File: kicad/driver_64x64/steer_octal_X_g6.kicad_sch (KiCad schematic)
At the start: 66 parts

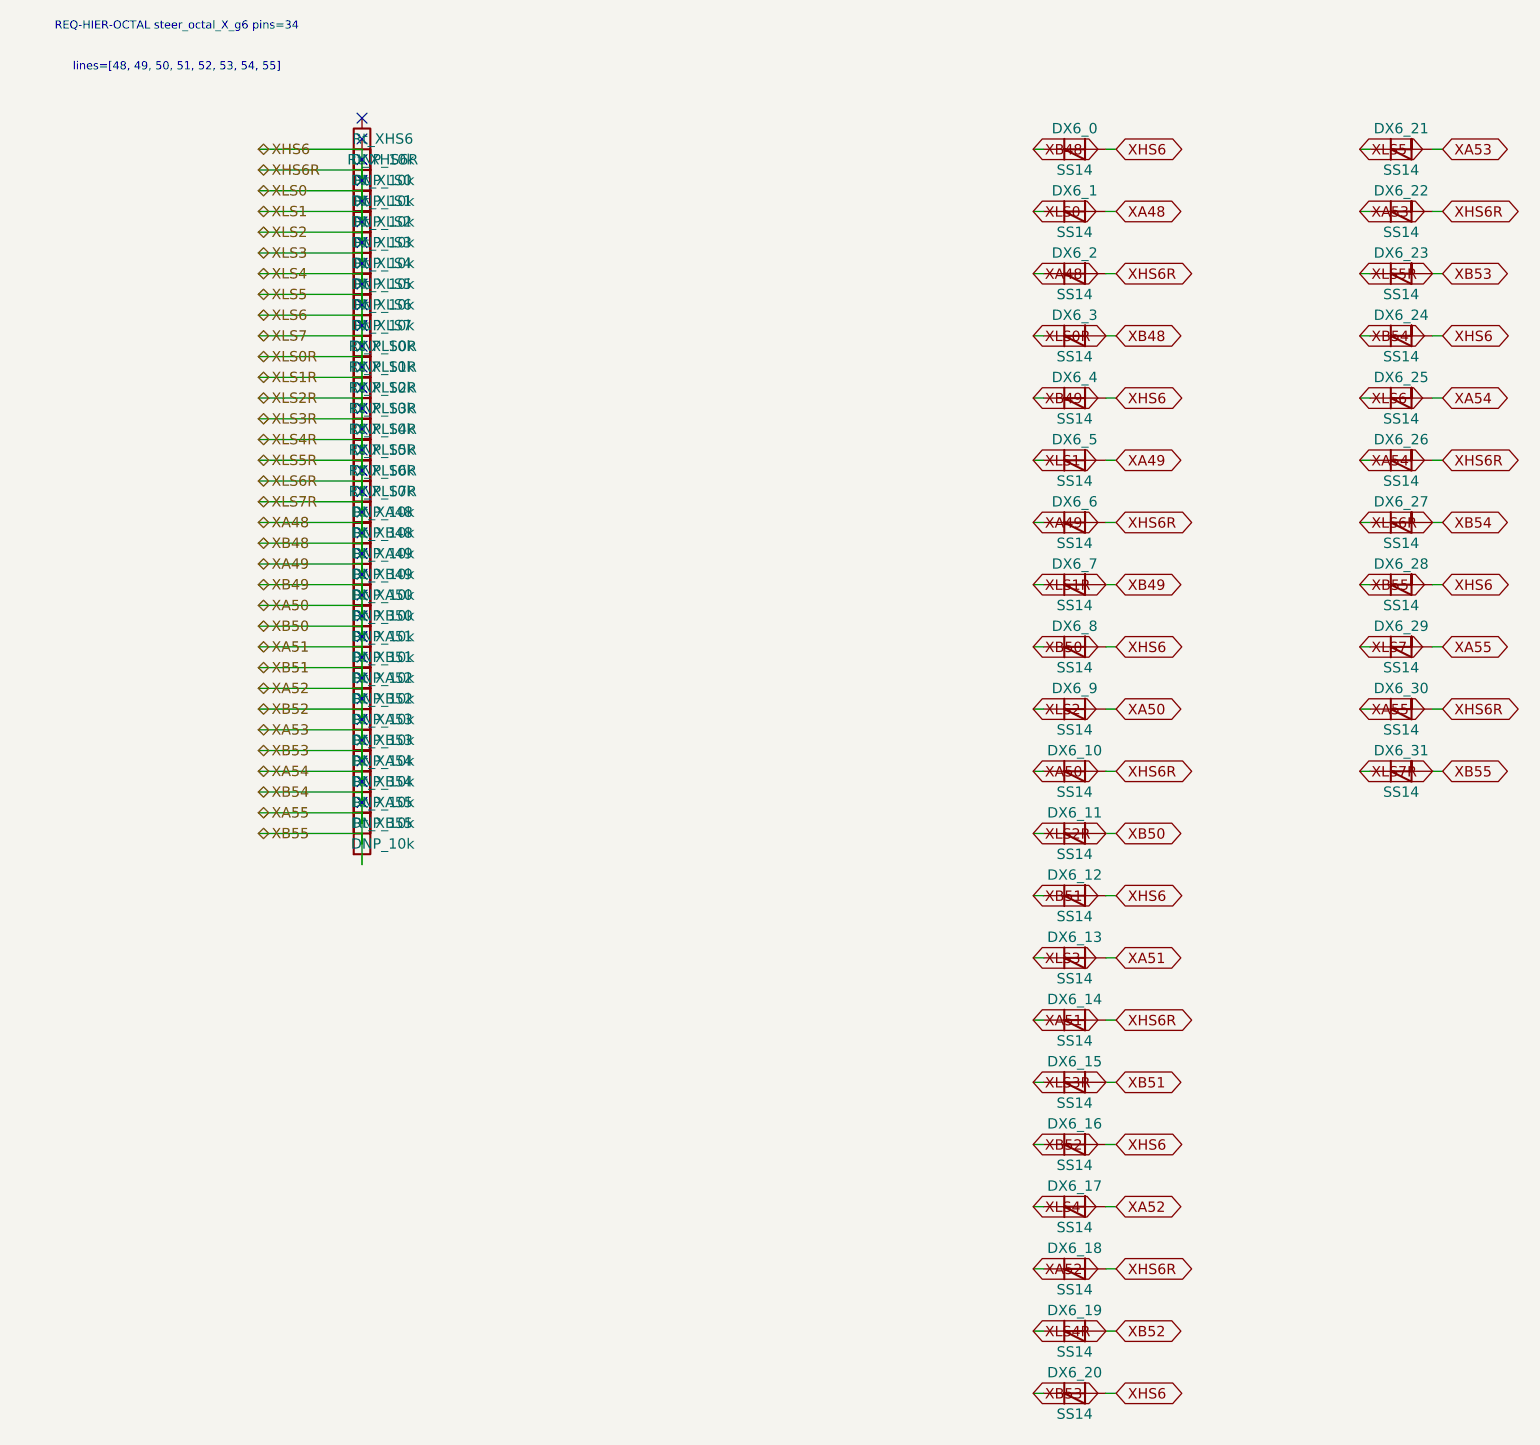
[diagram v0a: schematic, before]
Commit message: logical seperation into host and multiple decode/drive/steering boards
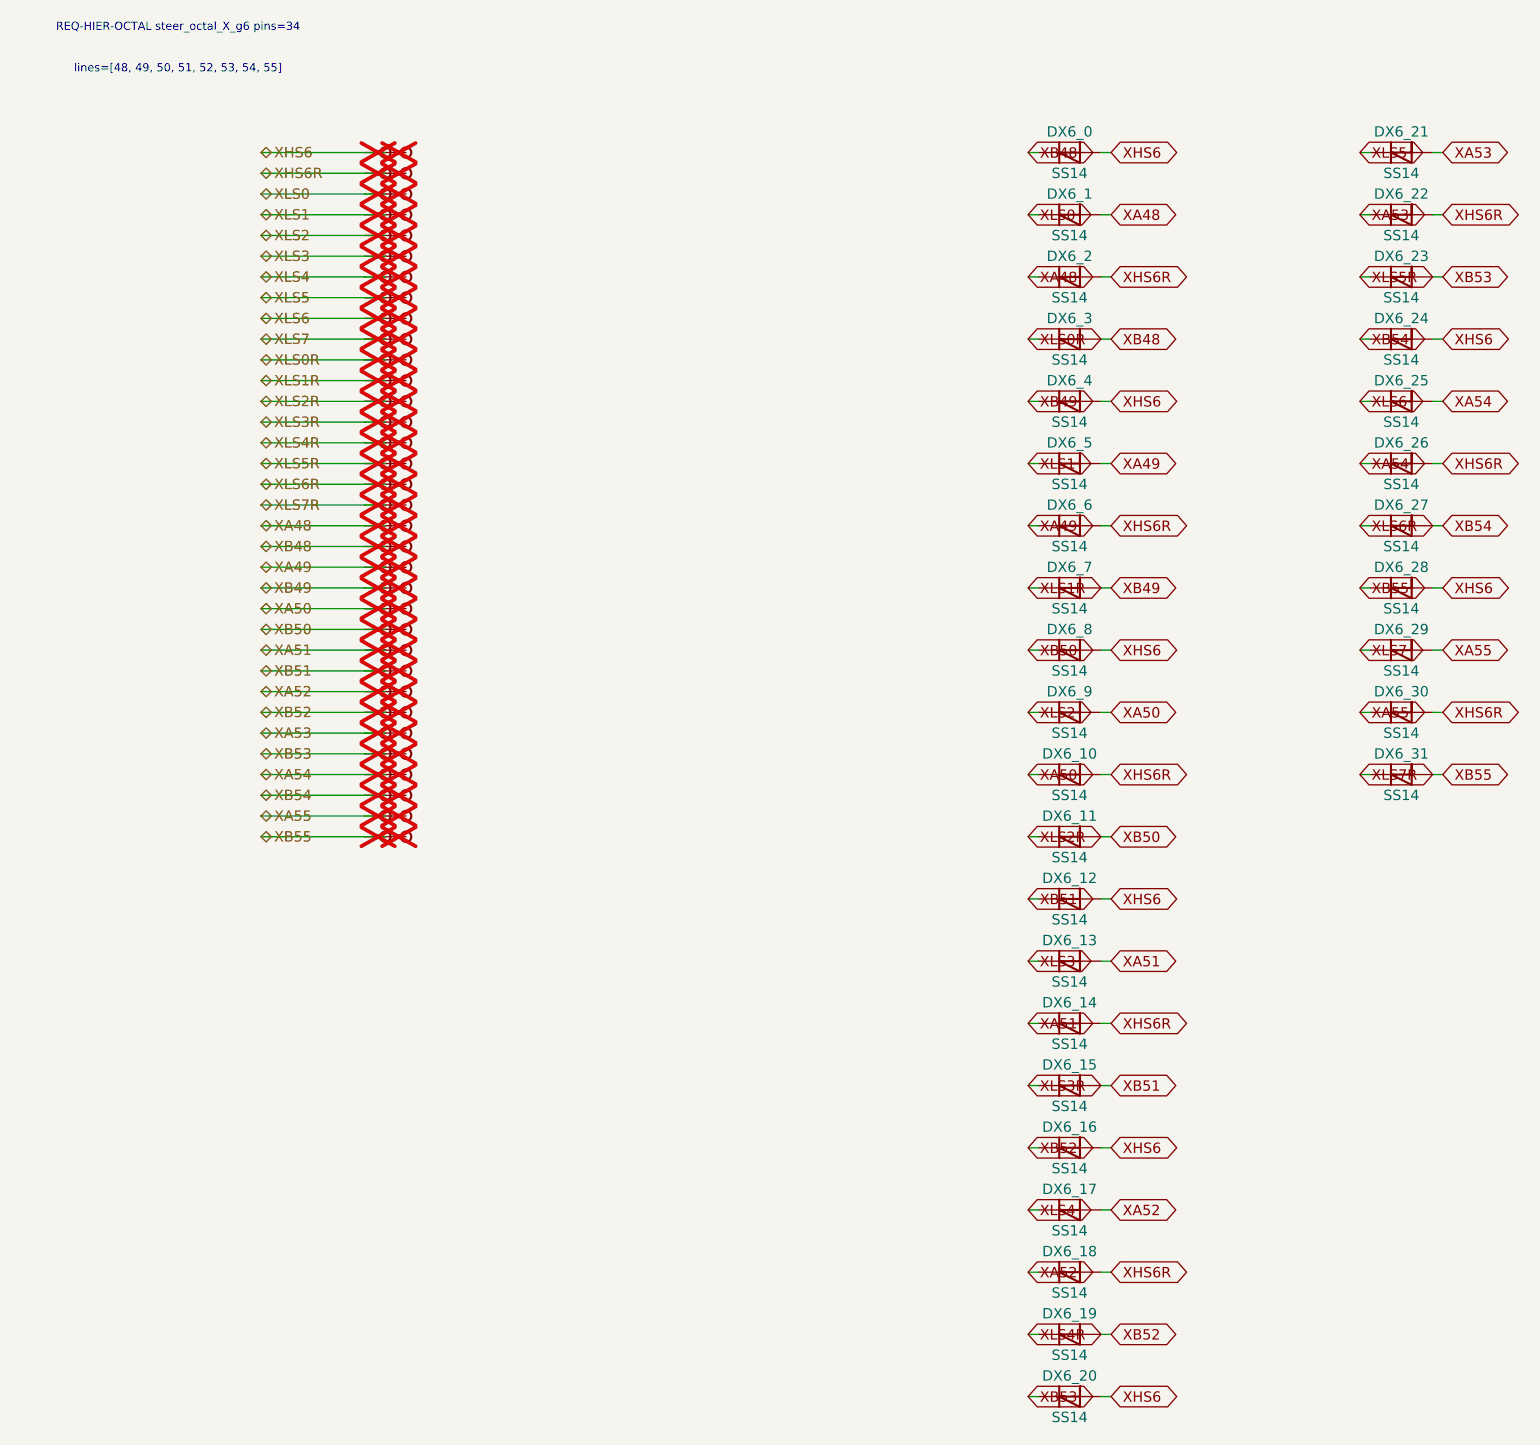
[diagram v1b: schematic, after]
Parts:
- removed Rt_XA48, Rt_XA49, Rt_XA50, Rt_XA51, Rt_XA52, Rt_XA53, Rt_XA54, Rt_XA55, Rt_XB48, Rt_XB49, Rt_XB50, Rt_XB51, Rt_XB52, Rt_XB53, Rt_XB54, Rt_XB55, Rt_XHS6, Rt_XHS6R, Rt_XLS0, Rt_XLS0R, Rt_XLS1, Rt_XLS1R, Rt_XLS2, Rt_XLS2R, Rt_XLS3, Rt_XLS3R, Rt_XLS4, Rt_XLS4R, Rt_XLS5, Rt_XLS5R, Rt_XLS6, Rt_XLS6R, Rt_XLS7, Rt_XLS7R: DNP_10k, symbol Device:R
- added TP_XA48, TP_XA48b, TP_XA49, TP_XA49b, TP_XA50, TP_XA50b, TP_XA51, TP_XA51b, TP_XA52, TP_XA52b, TP_XA53, TP_XA53b, TP_XA54, TP_XA54b, TP_XA55, TP_XA55b, TP_XB48, TP_XB48b, TP_XB49, TP_XB49b, TP_XB50, TP_XB50b, TP_XB51, TP_XB51b, TP_XB52, TP_XB52b, TP_XB53, TP_XB53b, TP_XB54, TP_XB54b, TP_XB55, TP_XB55b, TP_XHS6, TP_XHS6R, TP_XHS6Rb, TP_XHS6b, TP_XLS0, TP_XLS0R, TP_XLS0Rb, TP_XLS0b, TP_XLS1, TP_XLS1R, TP_XLS1Rb, TP_XLS1b, TP_XLS2, TP_XLS2R, TP_XLS2Rb, TP_XLS2b, TP_XLS3, TP_XLS3R, TP_XLS3Rb, TP_XLS3b, TP_XLS4, TP_XLS4R, TP_XLS4Rb, TP_XLS4b, TP_XLS5, TP_XLS5R, TP_XLS5Rb, TP_XLS5b, TP_XLS6, TP_XLS6R, TP_XLS6Rb, TP_XLS6b, TP_XLS7, TP_XLS7R, TP_XLS7Rb, TP_XLS7b: Stub, symbol CMR:Stub
- DX6_0, DX6_1, DX6_10, DX6_11, DX6_12, DX6_13, DX6_14, DX6_15, DX6_16, DX6_17, DX6_18, DX6_19, DX6_2, DX6_20, DX6_21, DX6_22, DX6_23, DX6_24, DX6_25, DX6_26, DX6_27, DX6_28, DX6_29, DX6_3, DX6_30, DX6_31, DX6_4, DX6_5, DX6_6, DX6_7, DX6_8, DX6_9: symbol Device:D_Schottky -> CMR:D_Schottky
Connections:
- net XA48: now also TP_XA48.1, TP_XA48b.1; no longer DX6_0.1 (K), DX6_0.2 (A), DX6_1.1 (K), DX6_10.1 (K), DX6_10.2 (A), DX6_11.1 (K), DX6_11.2 (A), DX6_12.1 (K), DX6_12.2 (A), DX6_13.1 (K), DX6_13.2 (A), DX6_14.1 (K), DX6_14.2 (A), DX6_15.1 (K), DX6_15.2 (A), DX6_16.1 (K), DX6_16.2 (A), DX6_17.1 (K), DX6_17.2 (A), DX6_18.1 (K), DX6_18.2 (A), DX6_19.1 (K), DX6_19.2 (A), DX6_2.2 (A), DX6_20.1 (K), DX6_20.2 (A), DX6_21.1 (K), DX6_21.2 (A), DX6_22.1 (K), DX6_22.2 (A), DX6_23.1 (K), DX6_23.2 (A), DX6_24.1 (K), DX6_24.2 (A), DX6_25.1 (K), DX6_25.2 (A), DX6_26.1 (K), DX6_26.2 (A), DX6_27.1 (K), DX6_27.2 (A), DX6_28.1 (K), DX6_28.2 (A), DX6_29.1 (K), DX6_29.2 (A), DX6_3.1 (K), DX6_3.2 (A), DX6_30.1 (K), DX6_30.2 (A), DX6_31.1 (K), DX6_31.2 (A), DX6_4.1 (K), DX6_4.2 (A), DX6_5.1 (K), DX6_5.2 (A), DX6_6.1 (K), DX6_6.2 (A), DX6_7.1 (K), DX6_7.2 (A), DX6_8.1 (K), DX6_8.2 (A), DX6_9.1 (K), DX6_9.2 (A)
- new net XA49: DX6_5.2 (A), DX6_6.1 (K), TP_XA49.1, TP_XA49b.1
- new net XA50: DX6_10.1 (K), DX6_9.2 (A), TP_XA50.1, TP_XA50b.1
- new net XA51: DX6_13.2 (A), DX6_14.1 (K), TP_XA51.1, TP_XA51b.1
- new net XA52: DX6_17.2 (A), DX6_18.1 (K), TP_XA52.1, TP_XA52b.1
- new net XA53: DX6_21.2 (A), DX6_22.1 (K), TP_XA53.1, TP_XA53b.1
- new net XA54: DX6_25.2 (A), DX6_26.1 (K), TP_XA54.1, TP_XA54b.1
- new net XA55: DX6_29.2 (A), DX6_30.1 (K), TP_XA55.1, TP_XA55b.1
- new net XB48: DX6_0.1 (K), DX6_3.2 (A), TP_XB48.1, TP_XB48b.1
- new net XB49: DX6_4.1 (K), DX6_7.2 (A), TP_XB49.1, TP_XB49b.1
- new net XB50: DX6_11.2 (A), DX6_8.1 (K), TP_XB50.1, TP_XB50b.1
- new net XB51: DX6_12.1 (K), DX6_15.2 (A), TP_XB51.1, TP_XB51b.1
- new net XB52: DX6_16.1 (K), DX6_19.2 (A), TP_XB52.1, TP_XB52b.1
- new net XB53: DX6_20.1 (K), DX6_23.2 (A), TP_XB53.1, TP_XB53b.1
- new net XB54: DX6_24.1 (K), DX6_27.2 (A), TP_XB54.1, TP_XB54b.1
- new net XB55: DX6_28.1 (K), DX6_31.2 (A), TP_XB55.1, TP_XB55b.1
- new net XHS6: DX6_0.2 (A), DX6_12.2 (A), DX6_16.2 (A), DX6_20.2 (A), DX6_24.2 (A), DX6_28.2 (A), DX6_4.2 (A), DX6_8.2 (A), TP_XHS6.1, TP_XHS6b.1
- new net XHS6R: DX6_10.2 (A), DX6_14.2 (A), DX6_18.2 (A), DX6_2.2 (A), DX6_22.2 (A), DX6_26.2 (A), DX6_30.2 (A), DX6_6.2 (A), TP_XHS6R.1, TP_XHS6Rb.1
- new net XLS0: DX6_1.1 (K), TP_XLS0.1, TP_XLS0b.1
- new net XLS0R: DX6_3.1 (K), TP_XLS0R.1, TP_XLS0Rb.1
- new net XLS1: DX6_5.1 (K), TP_XLS1.1, TP_XLS1b.1
- new net XLS1R: DX6_7.1 (K), TP_XLS1R.1, TP_XLS1Rb.1
- new net XLS2: DX6_9.1 (K), TP_XLS2.1, TP_XLS2b.1
- new net XLS2R: DX6_11.1 (K), TP_XLS2R.1, TP_XLS2Rb.1
- new net XLS3: DX6_13.1 (K), TP_XLS3.1, TP_XLS3b.1
- new net XLS3R: DX6_15.1 (K), TP_XLS3R.1, TP_XLS3Rb.1
- new net XLS4: DX6_17.1 (K), TP_XLS4.1, TP_XLS4b.1
- new net XLS4R: DX6_19.1 (K), TP_XLS4R.1, TP_XLS4Rb.1
- new net XLS5: DX6_21.1 (K), TP_XLS5.1, TP_XLS5b.1
- new net XLS5R: DX6_23.1 (K), TP_XLS5R.1, TP_XLS5Rb.1
- new net XLS6: DX6_25.1 (K), TP_XLS6.1, TP_XLS6b.1
- new net XLS6R: DX6_27.1 (K), TP_XLS6R.1, TP_XLS6Rb.1
- new net XLS7: DX6_29.1 (K), TP_XLS7.1, TP_XLS7b.1
- new net XLS7R: DX6_31.1 (K), TP_XLS7R.1, TP_XLS7Rb.1
- no-connect marks 34 -> 0
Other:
- moved on the sheet: DX6_0, DX6_1, DX6_10, DX6_11, DX6_12, DX6_13, DX6_14, DX6_15, DX6_16, DX6_17, DX6_18, DX6_19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
